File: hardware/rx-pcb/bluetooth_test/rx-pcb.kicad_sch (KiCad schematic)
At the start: 29 parts, among them J1 Conn_01x05_Pin, J2 Conn_01x04_Pin, J4 Conn_01x04_Pin, SW1 SW_SPST, U1 STM32WB05KZV6TR, U2 STS4L-AD1B-R3, U3 LMT70AYFQR, X1 Q22FA12800025, X2 ABS07-32.768KHZ-1-T

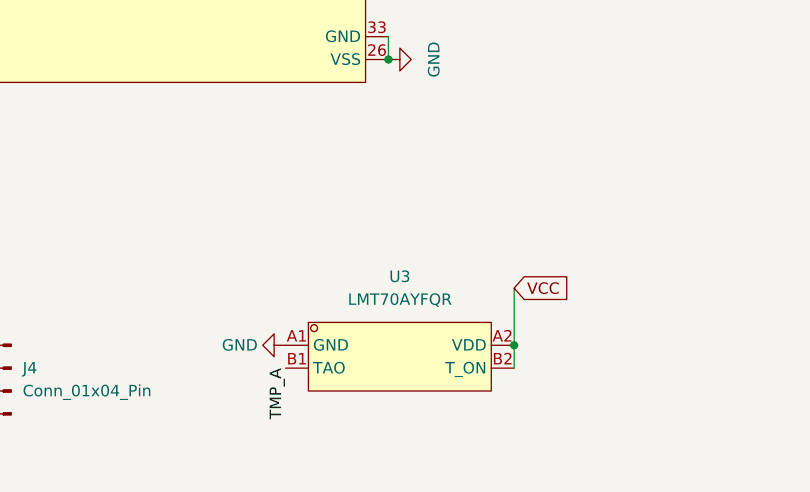
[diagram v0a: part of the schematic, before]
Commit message: fixed pwr header silkscreen mismatch. added reverse bias protection diode. added power good indicator diode for testing (DNP on final iteration)
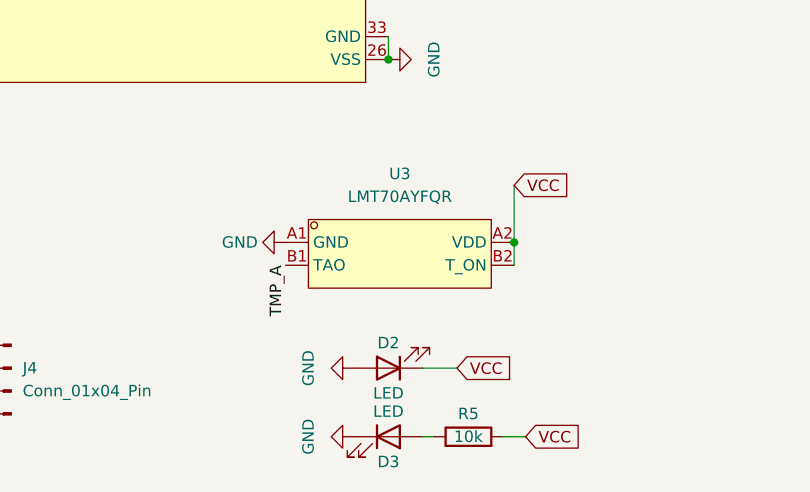
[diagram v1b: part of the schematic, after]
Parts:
- added D2, D3: LED, rx-parts:LED_0805_2012Metric_Pad1.15x1.40mm_HandSolder, symbol rx-parts:LED
- added R5: 10k, rx-parts:R_0805_2012Metric_Pad1.20x1.40mm_HandSolder, symbol rx-parts:R
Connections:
- net GND: now also D2.2 (A), D3.1 (K)
- net VCC: now also D2.1 (K), R5.2
- new net: D3.2 (A), R5.1
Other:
- moved on the sheet: U3
